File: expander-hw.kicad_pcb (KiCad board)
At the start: 2 copper layers, 15 parts, among them J1 Conn_ARM_JTAG_SWD_10, J2 USB_C_Receptacle_USB2.0_16P, J3 Conn_02x08_Odd_Even, U1 STM32H562RGTx, U2 SRDA3.3-4BTG, U3 AZ1117-3.3, U4 SRDA3.3-4BTG, U5 USBLC6-2SC6, U6 SRDA3.3-4BTG

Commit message: save
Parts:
- added C1: 100nF, Capacitor_SMD:C_0603_1608Metric, F.Cu at (126.0, 109.2)
- added C2: 100nF, Capacitor_SMD:C_0603_1608Metric, F.Cu at (135.8, 105.6)
- added C3: 100nF, Capacitor_SMD:C_0603_1608Metric, F.Cu at (136.2, 93.6)
- added C4: 100nF, Capacitor_SMD:C_0603_1608Metric, F.Cu at (121.2, 93.6)
- added R7: 10k, Resistor_SMD:R_0603_1608Metric, F.Cu at (128.0, 109.2)
- added X1: ECS-2520MV-xxx-xx, Crystal:Crystal_SMD_TXC_7M-4Pin_3.2x2.5mm, F.Cu at (137.6, 102.4)
- J3: footprint Connector_PinHeader_2.54mm:PinHeader_2x08_P2.54mm_Horizontal -> Connector_PinHeader_2.54mm:PinHeader_2x08_P2.54mm_Vertical
- R1, R2, R3, R4, R5, R6: footprint Resistor_SMD:R_0805_2012Metric -> Resistor_SMD:R_0603_1608Metric
- moved R1 64.0 mm to (111.2, 109.8), turned to 180 degrees
- moved R2 59.2 mm to (115.0, 109.8), turned to 180 degrees
- moved R3 44.3 mm to (134.8, 110.0), turned to -90 degrees
- moved R4 42.3 mm to (132.8, 109.2), turned to -90 degrees
- moved R5 36.7 mm to (137.2, 108.4), turned to 90 degrees
- moved U6 32.6 mm to (144.2, 108.8)
- moved U2 32.6 mm to (144.2, 102.8)
- moved R6 14.6 mm to (139.2, 107.6)
- moved U4 3.88 mm to (144.2, 96.8), turned to 0 degrees
- moved J1 2.14 mm to (118.6, 110.0)
- moved U1 1.52 mm to (128.8, 99.5)
- moved J3 1.45 mm to (150.0, 92.9)
- turned U5 to 180 degrees
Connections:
- J3 pad 1: /I2C1_SDA -> +3.3V
- J3 pad 10: unconnected-(J3-Pin_10-Pad10) -> /SPI2_CS
- J3 pad 11: unconnected-(J3-Pin_11-Pad11) -> GND
- J3 pad 12: unconnected-(J3-Pin_12-Pad12) -> GND
- J3 pad 13: unconnected-(J3-Pin_13-Pad13) -> /I2C3_SDA
- J3 pad 14: unconnected-(J3-Pin_14-Pad14) -> /I2C3_SCL
- J3 pad 15: unconnected-(J3-Pin_15-Pad15) -> /I2C1_SDA
- J3 pad 16: unconnected-(J3-Pin_16-Pad16) -> /I2C1_SCL
- J3 pad 2: /I2C3_SDA -> VBUS
- J3 pad 3: /I2C1_SCL -> /SPI1_SCK
- J3 pad 4: /I2C3_SCL -> /SPI1_MISO
- J3 pad 5: GND -> /SPI1_MOSI
- J3 pad 6: +3.3V -> /SPI1_CS
- J3 pad 7: GND -> /SPI2_SCK
- J3 pad 8: VBUS -> /SPI2_MISO
- J3 pad 9: unconnected-(J3-Pin_9-Pad9) -> /SPI2_MOSI
- R3 pad 2: Net-(U4-I/O1) -> /I2C1_SCL
- R4 pad 2: Net-(U4-I/O2) -> /I2C1_SDA
- R5 pad 2: Net-(U4-I/O3) -> /I2C3_SCL
- R6 pad 2: Net-(U4-I/O4) -> /I2C3_SDA
- U1 pad 10: unconnected-(U1-PC2-Pad10) -> /SPI2_MISO
- U1 pad 11: unconnected-(U1-PC3-Pad11) -> /SPI2_CS
- U1 pad 14: unconnected-(U1-PA0-Pad14) -> /SPI1_CS
- U1 pad 21: unconnected-(U1-PA5-Pad21) -> /SPI1_SCK
- U1 pad 22: unconnected-(U1-PA6-Pad22) -> /SPI1_MISO
- U1 pad 23: unconnected-(U1-PA7-Pad23) -> /SPI1_MOSI
- U1 pad 29: /I2C2_SCL -> /SPI2_SCK
- U1 pad 33: /I2C2_SDA -> unconnected-(U1-PB12-Pad33)
- U1 pad 5: unconnected-(U1-PH0-Pad5) -> /PH0
- U1 pad 6: unconnected-(U1-PH1-Pad6) -> /PH1
- U1 pad 60: unconnected-(U1-BOOT0-Pad60) -> Net-(U1-BOOT0)
- U1 pad 7: unconnected-(U1-NRST-Pad7) -> /~{RESET}
- U1 pad 9: unconnected-(U1-PC1-Pad9) -> /SPI2_MOSI
- U2 pad 1: unconnected-(U2-I/O1-Pad1) -> /SPI2_SCK
- U2 pad 4: unconnected-(U2-I/O2-Pad4) -> /SPI2_CS
- U2 pad 6: unconnected-(U2-I/O3-Pad6) -> /SPI2_MOSI
- U2 pad 7: unconnected-(U2-I/O4-Pad7) -> /SPI2_MISO
- U4 pad 1: Net-(U4-I/O1) -> /SPI1_SCK
- U4 pad 4: Net-(U4-I/O2) -> /SPI1_CS
- U4 pad 6: Net-(U4-I/O3) -> /SPI1_MOSI
- U4 pad 7: Net-(U4-I/O4) -> /SPI1_MISO
- U5 pad 1: Net-(J2-D--PadA7) -> /D-
- U5 pad 3: Net-(J2-D+-PadA6) -> /D+
- U5 pad 4: /D- -> Net-(J2-D--PadA7)
- U5 pad 6: /D+ -> Net-(J2-D+-PadA6)
- U6 pad 1: unconnected-(U6-I/O1-Pad1) -> /I2C3_SDA
- U6 pad 4: unconnected-(U6-I/O2-Pad4) -> /I2C1_SCL
- U6 pad 6: unconnected-(U6-I/O3-Pad6) -> /I2C1_SDA
- U6 pad 7: unconnected-(U6-I/O4-Pad7) -> /I2C3_SCL
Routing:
- net VBUS: track 0.00 -> 64.9 mm, vias 0 -> 6
- net GND: track 0.00 -> 37.1 mm, vias 0 -> 15
- net /I2C3_SCL: track 0.00 -> 34.1 mm, vias 0 -> 2
- net /I2C3_SDA: track 0.00 -> 30.6 mm, vias 0 -> 2
- net /SPI2_CS: track 0.00 -> 29.5 mm, vias 0 -> 2
- net /SPI2_SCK: track 0.00 -> 29.1 mm, vias 0 -> 2
- net /I2C1_SCL: track 0.00 -> 28.2 mm
- net /SPI1_MISO: track 0.00 -> 25.2 mm, vias 0 -> 2
- net /I2C1_SDA: track 0.00 -> 24.4 mm
- net /SPI1_SCK: track 0.00 -> 24.0 mm, vias 0 -> 2
- net /SPI1_MOSI: track 0.00 -> 23.4 mm, vias 0 -> 2
- net /SPI2_MISO: track 0.00 -> 20.2 mm
- net /SPI1_CS: track 0.00 -> 19.8 mm
- net /~{RESET}: track 0.00 -> 17.9 mm, vias 0 -> 1
- net /SPI2_MOSI: track 0.00 -> 17.5 mm
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
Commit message: Complete v1
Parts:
- added C5: 10uF, Capacitor_SMD:C_0805_2012Metric, F.Cu at (117.4, 96.4)
- added C6: 10uF, Capacitor_SMD:C_0805_2012Metric, F.Cu at (139.2, 94.6)
- added C7: 10uF, Capacitor_SMD:C_0805_2012Metric, F.Cu at (120.6, 96.5)
- added C8: 10uF, Capacitor_SMD:C_0805_2012Metric, F.Cu at (117.4, 93.4)
- moved C4 0.20 mm to (121.2, 93.4)
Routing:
- net GND: track 37.1 -> 41.8 mm, vias 15 -> 18
- net VBUS: track 64.9 -> 66.2 mm

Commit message: save
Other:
- board outline added: 80 x 50 mm

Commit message: Add LED
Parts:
- added D1: LED, LED_SMD:LED_0603_1608Metric, F.Cu at (145.2, 92.6)
- added R8: 470, Resistor_SMD:R_0603_1608Metric, F.Cu at (142.0, 92.6)
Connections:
- U1 pad 17: unconnected-(U1-PA3-Pad17) -> /LED_HRTB
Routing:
- net /LED_HRTB: track 0.00 -> 10.5 mm, vias 0 -> 2
- net GND: track 41.8 -> 43.5 mm
- net Net-(D1-A): track 0.00 -> 1.61 mm

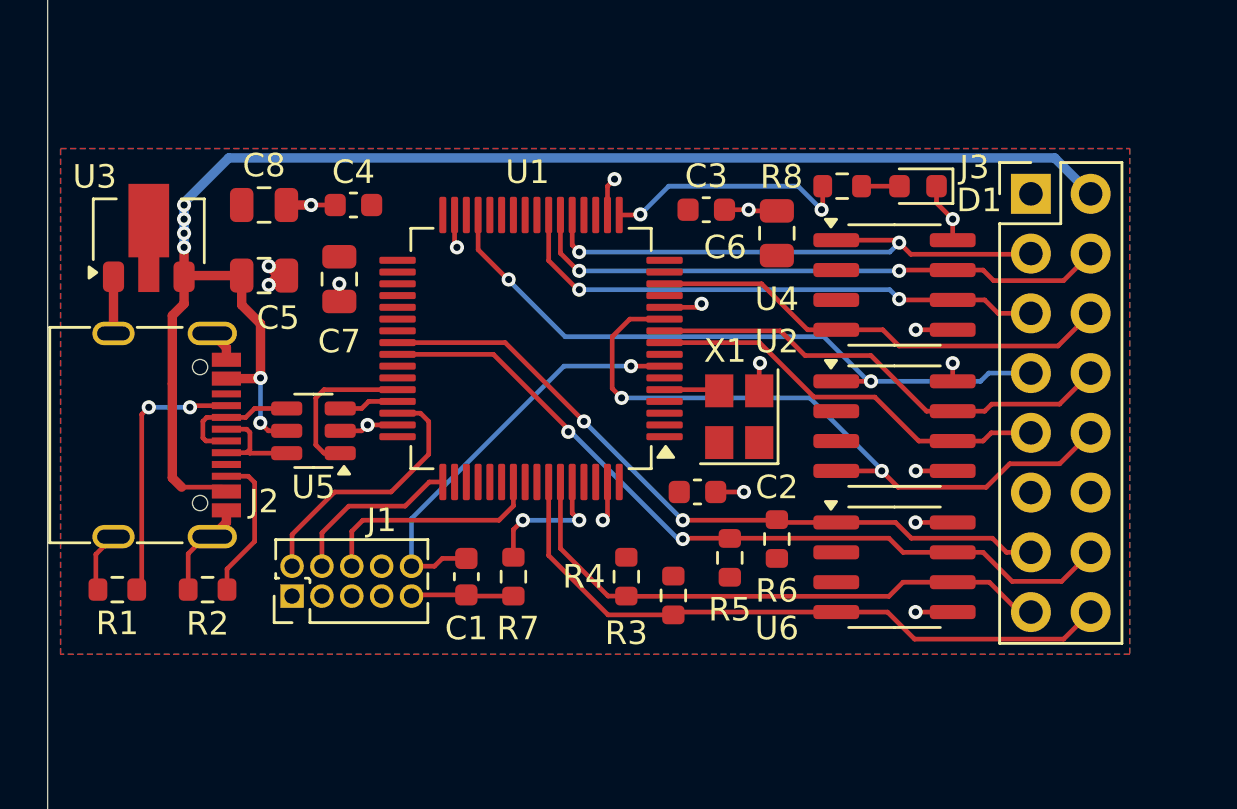
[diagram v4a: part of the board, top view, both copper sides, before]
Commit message: Fix vreg package
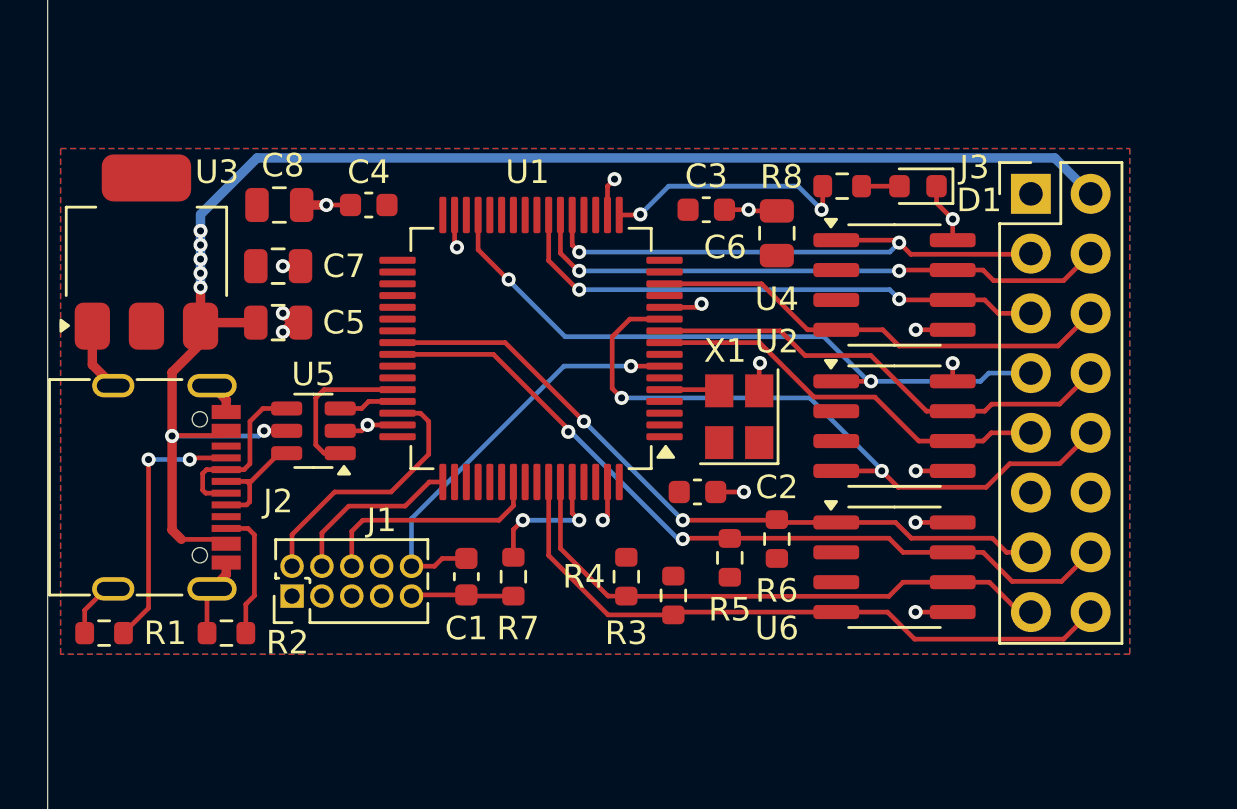
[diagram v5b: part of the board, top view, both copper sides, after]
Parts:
- U3: footprint Package_TO_SOT_SMD:SOT-89-3 -> Package_TO_SOT_SMD:SOT-223-3_TabPin2
- moved C7 2.66 mm to (118.0, 96.0), turned to 0 degrees
- moved J2 2.22 mm to (112.1, 105.4)
- moved C5 2.09 mm to (118.0, 98.4)
- moved R2 2.02 mm to (115.8, 111.6)
- moved R1 1.93 mm to (110.6, 111.6)
- moved U3 0.91 mm to (112.4, 95.4)
- moved C4 0.65 mm to (121.8, 93.4)
- moved C8 0.65 mm to (118.0, 93.4)
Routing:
- net Net-(J2-D--PadA7): track 5.55 -> 7.53 mm
- net Net-(J2-CC2): track 6.35 -> 5.64 mm
- net Net-(J2-D+-PadA6): track 4.51 -> 5.04 mm
- net VBUS: track 66.2 -> 65.7 mm, vias 6 -> 7

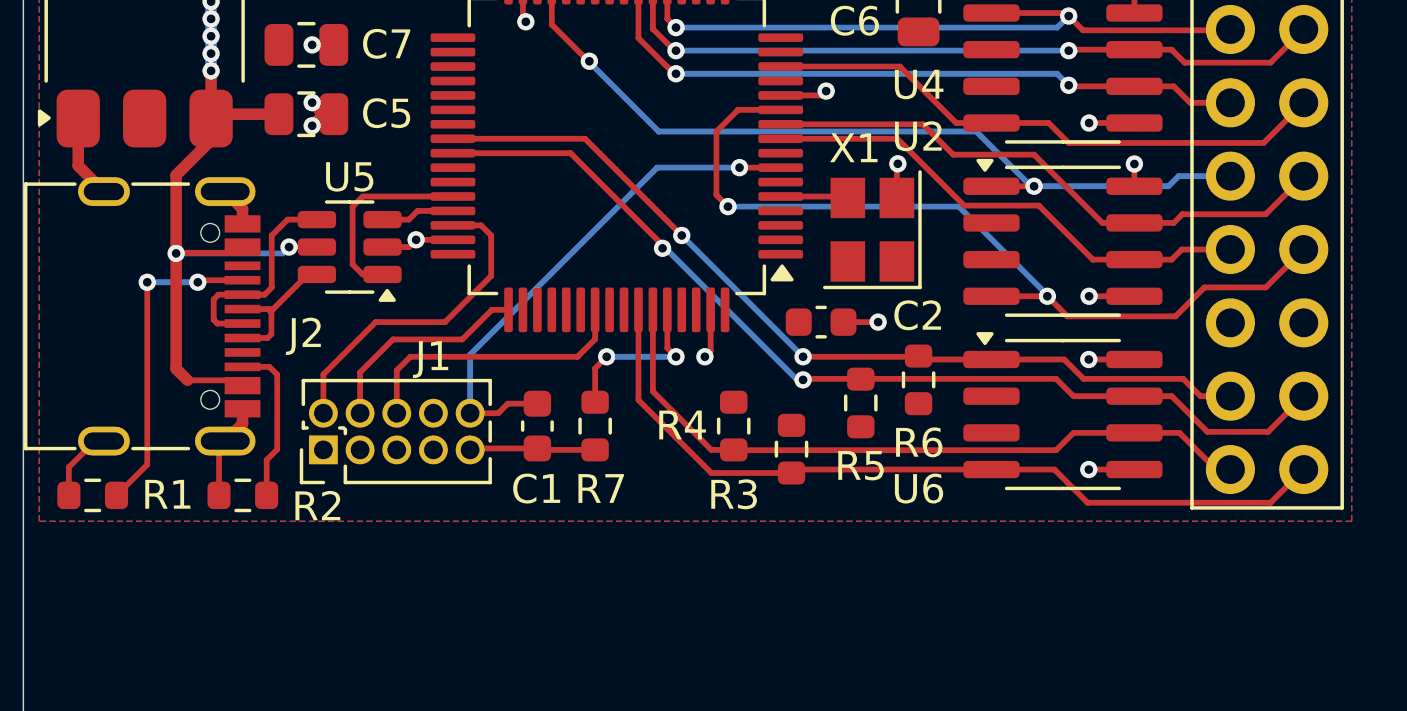
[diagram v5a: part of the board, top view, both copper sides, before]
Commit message: Fix USB lines
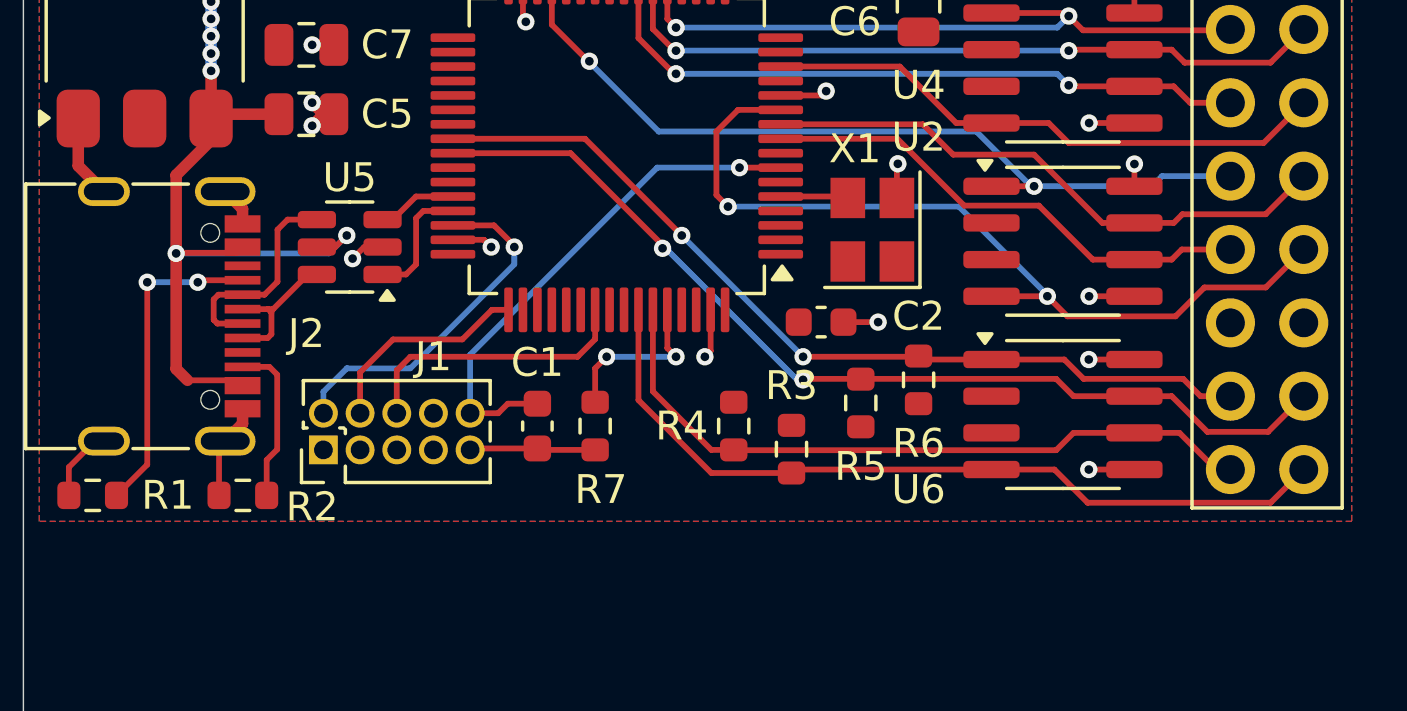
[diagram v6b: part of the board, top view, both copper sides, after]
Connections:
- U5 pad 1: /D- -> /D+
- U5 pad 3: /D+ -> /D-
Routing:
- net /D-: track 6.80 -> 2.77 mm
- net VBUS: track 65.7 -> 68.1 mm
- net /D+: track 2.56 -> 4.29 mm
- net /SWDIO: track 11.4 -> 12.2 mm, vias 0 -> 1
- net GND: track 43.4 -> 43.5 mm, vias 18 -> 19

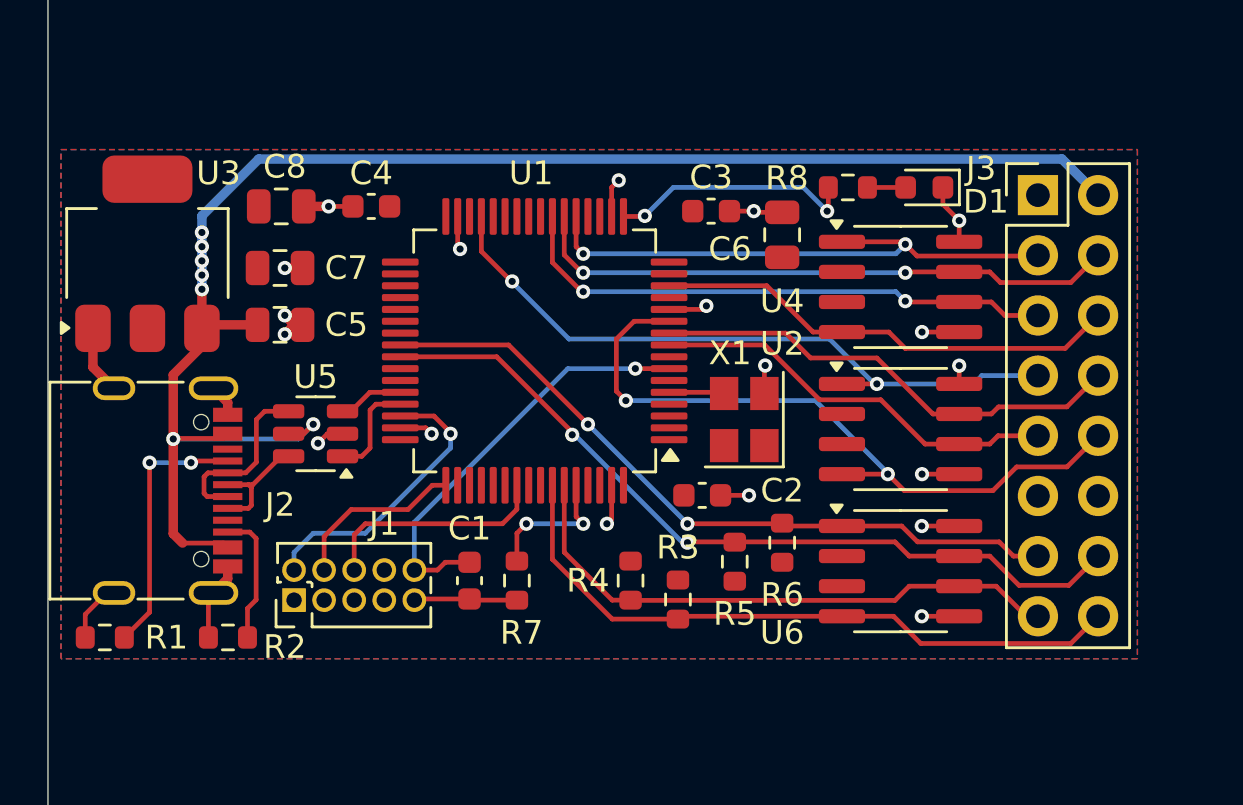
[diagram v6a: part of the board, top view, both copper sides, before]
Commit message: Move to STM32U545
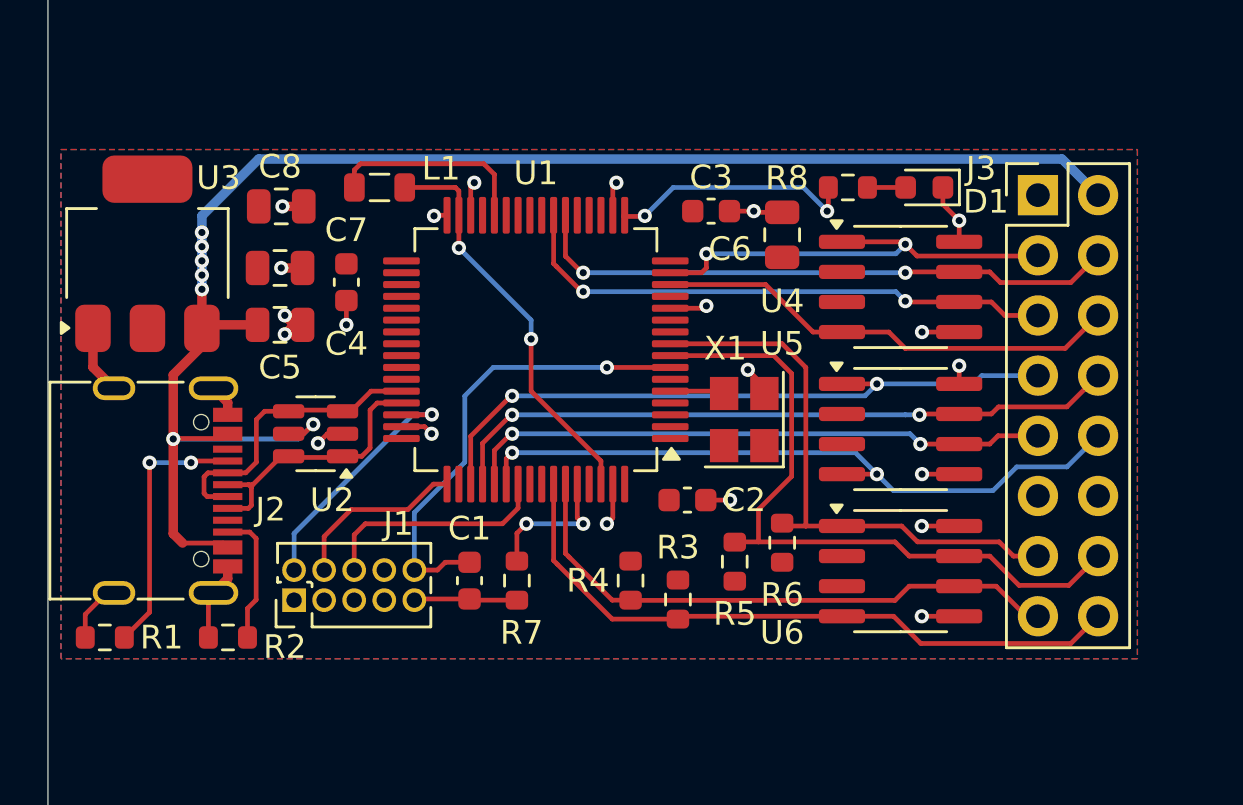
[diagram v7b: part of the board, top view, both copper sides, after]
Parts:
- added L1: 2.2uH, Inductor_SMD:L_0805_2012Metric, F.Cu at (122.2, 92.6)
- U1: value STM32H562RGTx -> STM32U545RETxQ
- moved C4 3.37 mm to (120.8, 96.6), turned to -90 degrees
- moved C2 0.66 mm to (135.2, 105.8)
- moved U1 0.07 mm to (128.8, 99.5)
- renumbered U5 to U2, U2 to U5
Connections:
- J2 pad A6: Net-(J2-D+-PadA6) -> /D+
- J2 pad A7: Net-(J2-D--PadA7) -> /D-
- J2 pad B6: Net-(J2-D+-PadA6) -> /D+
- J2 pad B7: Net-(J2-D--PadA7) -> /D-
- J3 pad 10: /SPI2_CS -> /SPI3_CS
- J3 pad 7: /SPI2_SCK -> /SPI3_SCK
- J3 pad 8: /SPI2_MISO -> /SPI3_MISO
- J3 pad 9: /SPI2_MOSI -> /SPI3_MOSI
- U1 pad 10: /SPI2_MISO -> unconnected-(U1-PC2-Pad10)
- U1 pad 11: /SPI2_CS -> unconnected-(U1-PC3-Pad11)
- U1 pad 15: unconnected-(U1-PA1-Pad15) -> /SPI1_SCK
- U1 pad 21: /SPI1_SCK -> unconnected-(U1-PA5-Pad21)
- U1 pad 28: unconnected-(U1-PB2-Pad28) -> Net-(U1-VLXSMPS)
- U1 pad 29: /SPI2_SCK -> +3.3V
- U1 pad 30: unconnected-(U1-VCAP-Pad30) -> GND
- U1 pad 31: GND -> Net-(L1-Pad2)
- U1 pad 32: +3.3V -> GND
- U1 pad 33: unconnected-(U1-PB12-Pad33) -> +3.3V
- U1 pad 40: /I2C3_SDA -> unconnected-(U1-PC9-Pad40)
- U1 pad 41: /I2C3_SCL -> unconnected-(U1-PA8-Pad41)
- U1 pad 51: unconnected-(U1-PC10-Pad51) -> /SPI3_SCK
- U1 pad 52: unconnected-(U1-PC11-Pad52) -> /SPI3_MISO
- U1 pad 53: unconnected-(U1-PC12-Pad53) -> /SPI3_MOSI
- U1 pad 54: unconnected-(U1-PD2-Pad54) -> /SPI3_CS
- U1 pad 62: unconnected-(U1-VCAP-Pad62) -> Net-(L1-Pad2)
- U1 pad 8: unconnected-(U1-PC0-Pad8) -> /I2C3_SCL
- U1 pad 9: /SPI2_MOSI -> /I2C3_SDA
- U2 pad 4: Net-(J2-D--PadA7) -> /D-
- U2 pad 6: Net-(J2-D+-PadA6) -> /D+
- U5 pad 1: /SPI2_SCK -> /SPI3_SCK
- U5 pad 4: /SPI2_CS -> /SPI3_CS
- U5 pad 6: /SPI2_MOSI -> /SPI3_MOSI
- U5 pad 7: /SPI2_MISO -> /SPI3_MISO
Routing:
- net /SPI2_CS: track 29.7 -> 0.00 mm, vias 2 -> 0
- net /SPI3_CS: track 0.00 -> 29.3 mm, vias 0 -> 2
- net /SPI2_SCK: track 29.1 -> 0.00 mm, vias 2 -> 0
- net /SPI3_MISO: track 0.00 -> 28.9 mm, vias 0 -> 2
- net /SPI3_SCK: track 0.00 -> 28.8 mm, vias 0 -> 2
- net /SPI3_MOSI: track 0.00 -> 25.0 mm, vias 0 -> 2
- net /SPI2_MISO: track 20.2 -> 0.00 mm
- net /SPI2_MOSI: track 17.5 -> 0.00 mm
- net Net-(L1-Pad2): track 0.00 -> 17.2 mm, vias 0 -> 2
- net /D-: track 2.77 -> 12.7 mm
- net Net-(U1-VLXSMPS): track 0.00 -> 8.67 mm
- net Net-(J2-D--PadA7): track 7.53 -> 0.00 mm
- net /D+: track 4.29 -> 11.7 mm
- net /I2C3_SDA: track 30.6 -> 24.2 mm, vias 2 -> 0
- net Net-(J2-D+-PadA6): track 5.04 -> 0.00 mm
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
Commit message: V2
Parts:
- added C9: 100nF, Capacitor_SMD:C_0603_1608Metric, F.Cu at (128.8, 92.0)
- moved D1 27.8 mm to (120.8, 106.0)
- moved R8 27.5 mm to (118.4, 106.8), turned to 90 degrees
- moved J1 1.80 mm to (120.0, 111.1)
- moved C1 1.70 mm to (127.2, 110.4)
- moved R7 1.54 mm to (129.0, 110.4)
- moved R2 0.40 mm to (115.4, 111.6)
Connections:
- U1 pad 17: /LED_HRTB -> unconnected-(U1-PA3-Pad17)
- U1 pad 42: unconnected-(U1-PA9-Pad42) -> /LED_HRTB
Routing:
- net /SWDIO: track 10.7 -> 13.3 mm
- net /SWO: track 9.89 -> 7.99 mm
- net /SWDCLK: track 7.52 -> 6.22 mm
- net Net-(U1-PH3): track 5.83 -> 6.61 mm
- net Net-(U1-VLXSMPS): track 8.67 -> 9.37 mm
- net GND: track 43.6 -> 43.2 mm, vias 21 -> 23
